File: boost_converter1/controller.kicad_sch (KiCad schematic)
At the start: 1 part, among them U2 STM32G474RETx

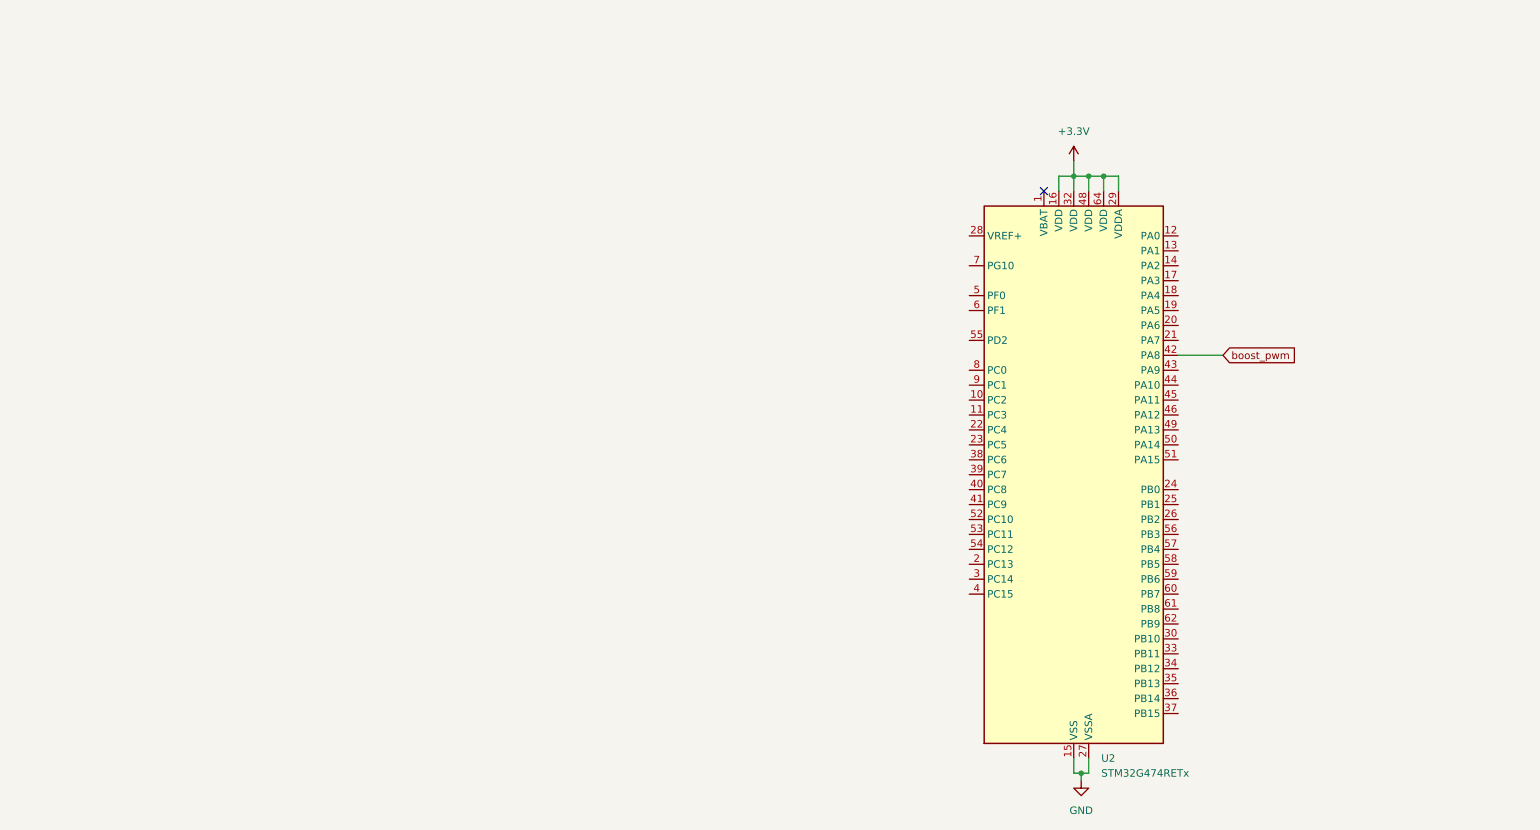
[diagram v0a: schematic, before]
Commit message: Updated components and footprints for power stage.
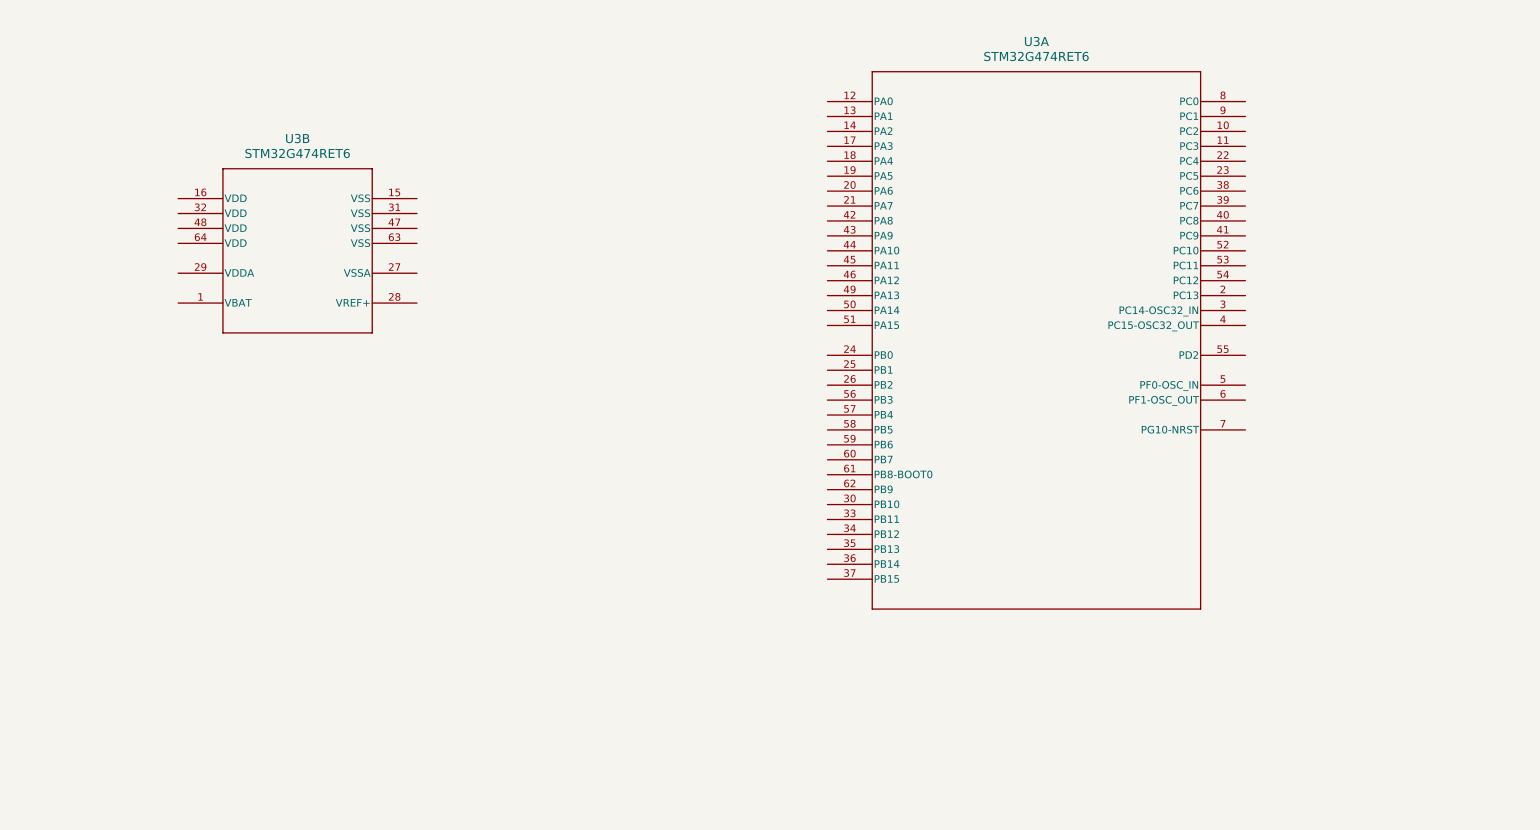
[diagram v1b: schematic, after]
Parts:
- removed U2: STM32G474RETx, Package_QFP:LQFP-64_10x10mm_P0.5mm, symbol MCU_ST_STM32G4:STM32G474RETx
- added U3: STM32G474RET6, LQFP64-10x10mm, symbol STM32G474RET6:STM32G474RET6
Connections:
- no-connect marks 1 -> 0

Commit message: [HW] Added MCU supporting components and programming connector.
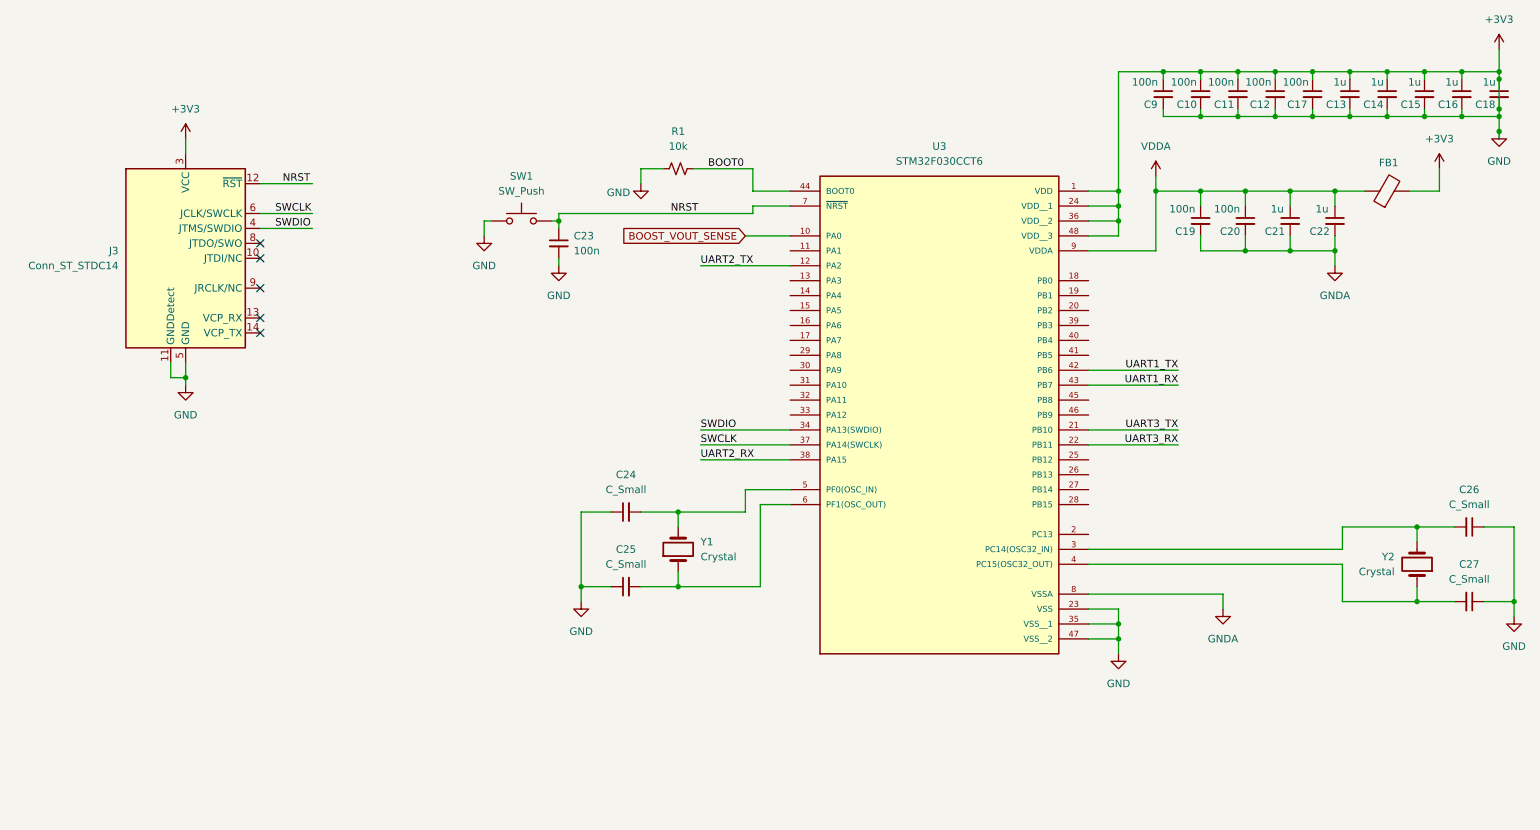
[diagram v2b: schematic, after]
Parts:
- removed U3: STM32G474RET6, LQFP64-10x10mm, symbol STM32G474RET6:STM32G474RET6
- added C10, C11, C12, C17, C19, C20, C23, C9: 100n, symbol Device:C_Small
- added C13, C14, C15, C16, C18, C21, C22: 1u, symbol Device:C_Small
- added C24, C25, C26, C27: C_Small, symbol Device:C_Small
- added FB1: FerriteBead, symbol Device:FerriteBead
- added J3: Conn_ST_STDC14, symbol Connector:Conn_ST_STDC14
- added R1: 10k, symbol Device:R_Small_US
- added SW1: SW_Push, symbol Switch:SW_Push
- added U3: STM32F030CCT6, STM32F030CCT6:QFP50P900X900X160-48N, symbol STM32F030CCT6:STM32F030CCT6
- added Y1, Y2: Crystal, symbol Device:Crystal
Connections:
- new net: C27.2, U3.4 (PC15(OSC32_OUT)), Y2.1
- new net: C26.2, U3.3 (PC14(OSC32_IN)), Y2.2
- new net: C25.2, U3.6 (PF1(OSC_OUT)), Y1.1
- new net: C24.2, U3.5 (PF0(OSC_IN)), Y1.2
- new net +3V3: C10.1, C10.2, C11.1, C11.2, C12.1, C12.2, C13.1, C13.2, C14.1, C14.2, C15.1, C15.2, C16.1, C16.2, C17.1, C17.2, C18.1, C18.2, C23.2, C24.1, C25.1, C26.1, C27.1, C9.1, C9.2, FB1.2, J3.11 (GNDDetect), J3.3 (VCC), J3.5 (GND), J3.7 (GND), R1.1, SW1.1, U3.1 (VDD), U3.23 (VSS), U3.24 (VDD__1), U3.35 (VSS__1), U3.36 (VDD__2), U3.47 (VSS__2), U3.48 (VDD__3)
- new net BOOST_VOUT_SENSE: U3.10 (PA0)
- new net BOOT0: R1.2, U3.44 (BOOT0)
- new net GNDA: C19.2, C20.2, C21.2, C22.2, U3.8 (VSSA)
- new net NRST: C23.1, J3.12 (~{RST}), SW1.2, U3.7 (~{NRST})
- new net SWCLK: J3.6 (JCLK/SWCLK), U3.37 (PA14(SWCLK))
- new net SWDIO: J3.4 (JTMS/SWDIO), U3.34 (PA13(SWDIO))
- new net UART1_RX: U3.43 (PB7)
- new net UART1_TX: U3.42 (PB6)
- new net UART2_RX: U3.38 (PA15)
- new net UART2_TX: U3.12 (PA2)
- new net UART3_RX: U3.22 (PB11)
- new net UART3_TX: U3.21 (PB10)
- new net VDDA: C19.1, C20.1, C21.1, C22.1, FB1.1, U3.9 (VDDA)
- no-connect marks 0 -> 5

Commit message: Maintenance
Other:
- note added: "Programming Connector"
- note added: "this uart is for tuning the control loop"
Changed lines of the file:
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@@
 	(generator_version "9.0")
 	(paper "A4")
+	(text "Programming Connector\n"
+		(exclude_from_sim no)
+		(at 41.402 29.464 0)
+		(effects
+			(font
+				(size 1.27 1.27)
+			)
+		)
+	)
+	(text "this uart is for tuning the control loop\n"
+		(exclude_from_sim no)
+		(at 229.87 88.392 0)
+		(effects
+			(font
+				(size 1.27 1.27)
+			)
+		)
+	)
 	(junction
 		(at 265.43 36.83)
